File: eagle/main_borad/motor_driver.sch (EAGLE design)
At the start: 18 parts, among them IC1 MEGA8-AI

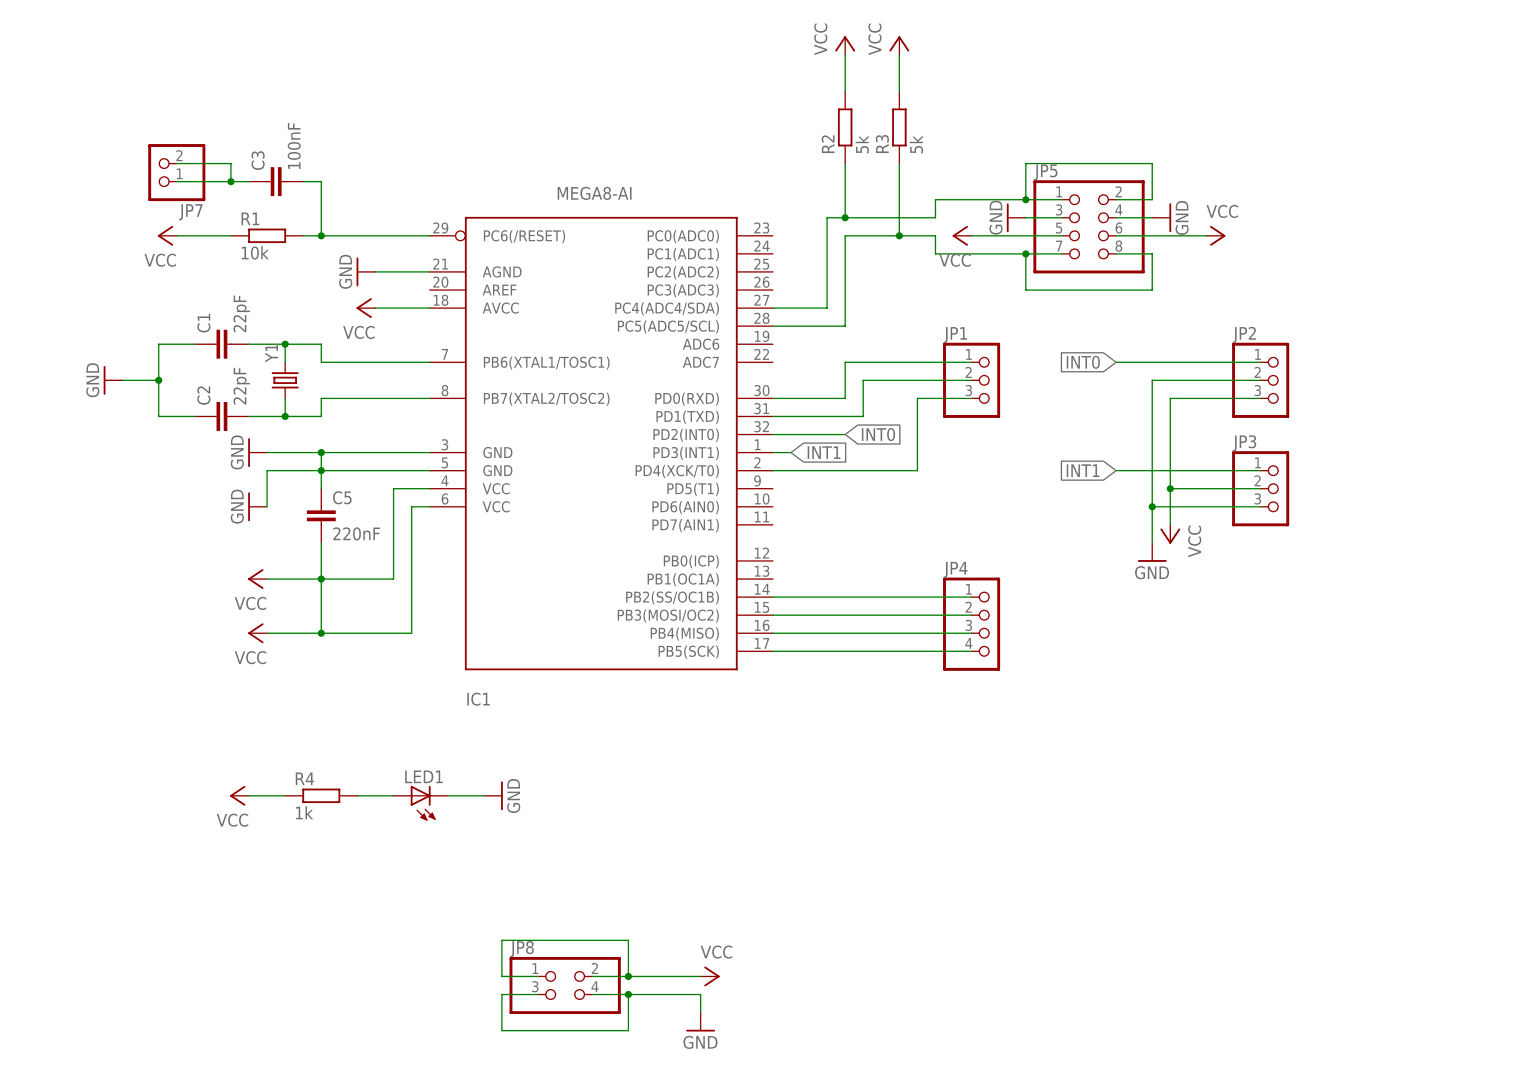
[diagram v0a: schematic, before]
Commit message: robot_driver updated
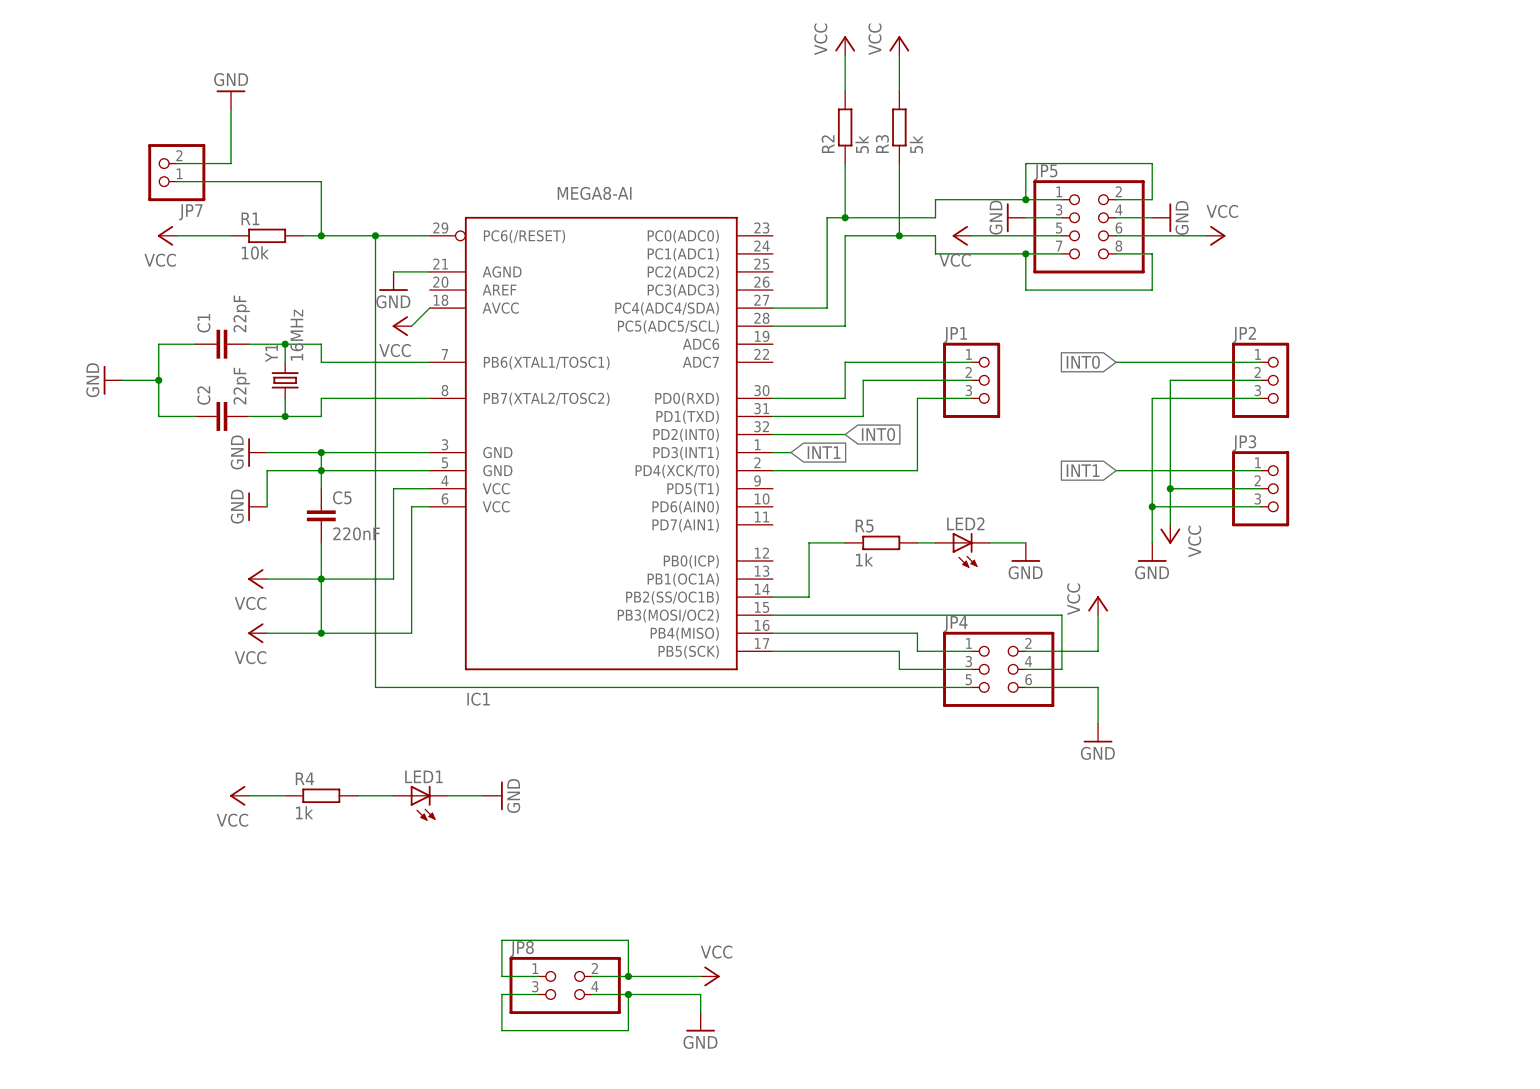
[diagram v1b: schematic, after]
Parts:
- removed C3: 100nF, SparkFun-Capacitors:CAP1206
- added LED2: (no value), adafruit:LEDCHIPLED_0805
- added R5: 1k, eagle-ltspice:R
- JP4: device pinhead:PINHD-1X4 -> pinhead:PINHD-2X3
- Y1: value (none) -> 16MHz
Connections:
- removed net N$15: IC1.PB2(SS/OC1B), JP4.1
- new net N$14: LED2.A, R5.2
- net GND: now also JP2.3, JP4.6, JP7.2, LED2.C; no longer JP2.2
- net N$12: now also JP4.3; no longer JP4.4
- net N$13: now also JP4.1; no longer JP4.3
- net N$4: now also IC1.PB2(SS/OC1B), R5.1; no longer C3.2, IC1.PC6(/RESET), R1.2
- net N$7: now also JP4.4; no longer JP4.2
- net RESET: now also IC1.PC6(/RESET), JP4.5, R1.2; no longer C3.1, JP7.2
- net VCC: now also JP2.2, JP4.2; no longer JP2.3

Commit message: otor_driver - led resistors updated
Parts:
- R4: value 1k -> 150k
- R5: value 1k -> 22k
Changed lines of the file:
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@@
 <part name="LED1" library="adafruit" deviceset="LED" device="CHIPLED_0805"/>
 <part name="GND9" library="supply1" deviceset="GND" device=""/>
-<part name="R4" library="eagle-ltspice" deviceset="R" device="" value="1k"/>
+<part name="R4" library="eagle-ltspice" deviceset="R" device="" value="150k"/>
 <part name="P+11" library="supply1" deviceset="VCC" device=""/>
 <part name="GND10" library="supply1" deviceset="GND" device=""/>
@@
 <part name="GND11" library="supply1" deviceset="GND" device=""/>
 <part name="P+12" library="supply1" deviceset="VCC" device=""/>
-<part name="R5" library="eagle-ltspice" deviceset="R" device="" value="1k"/>
+<part name="R5" library="eagle-ltspice" deviceset="R" device="" value="22k"/>
 <part name="LED2" library="adafruit" deviceset="LED" device="CHIPLED_0805"/>
 <part name="GND12" library="supply1" deviceset="GND" device=""/>

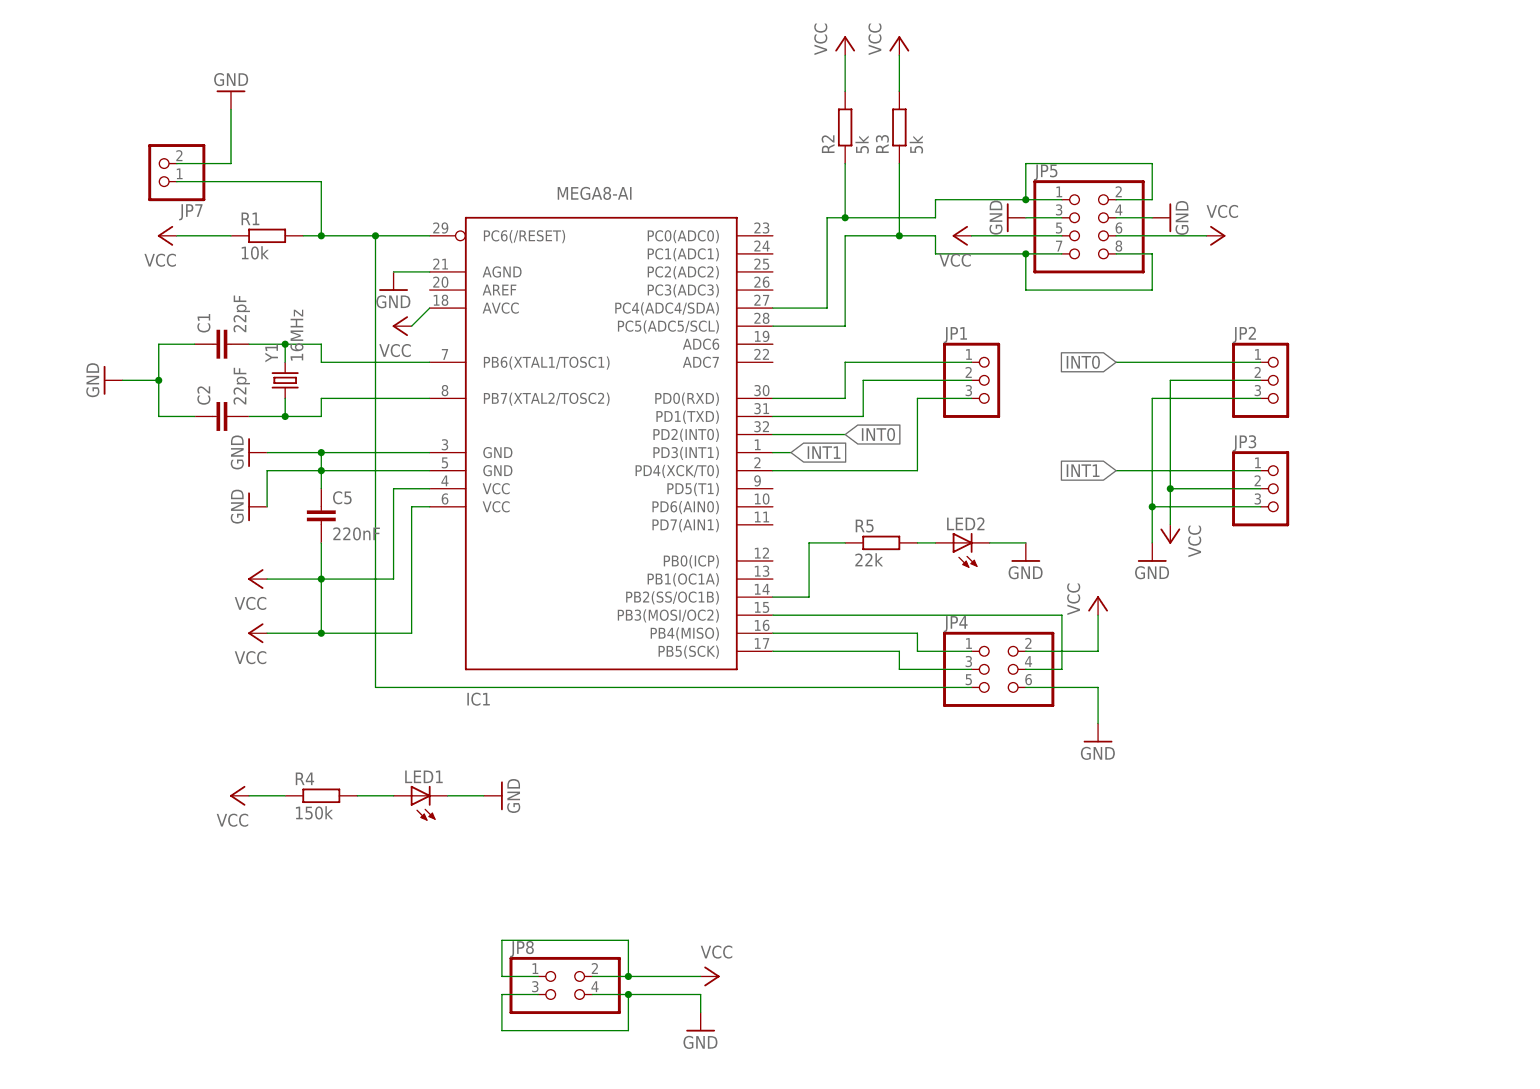
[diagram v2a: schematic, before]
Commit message: Repaired motor_driver PCB
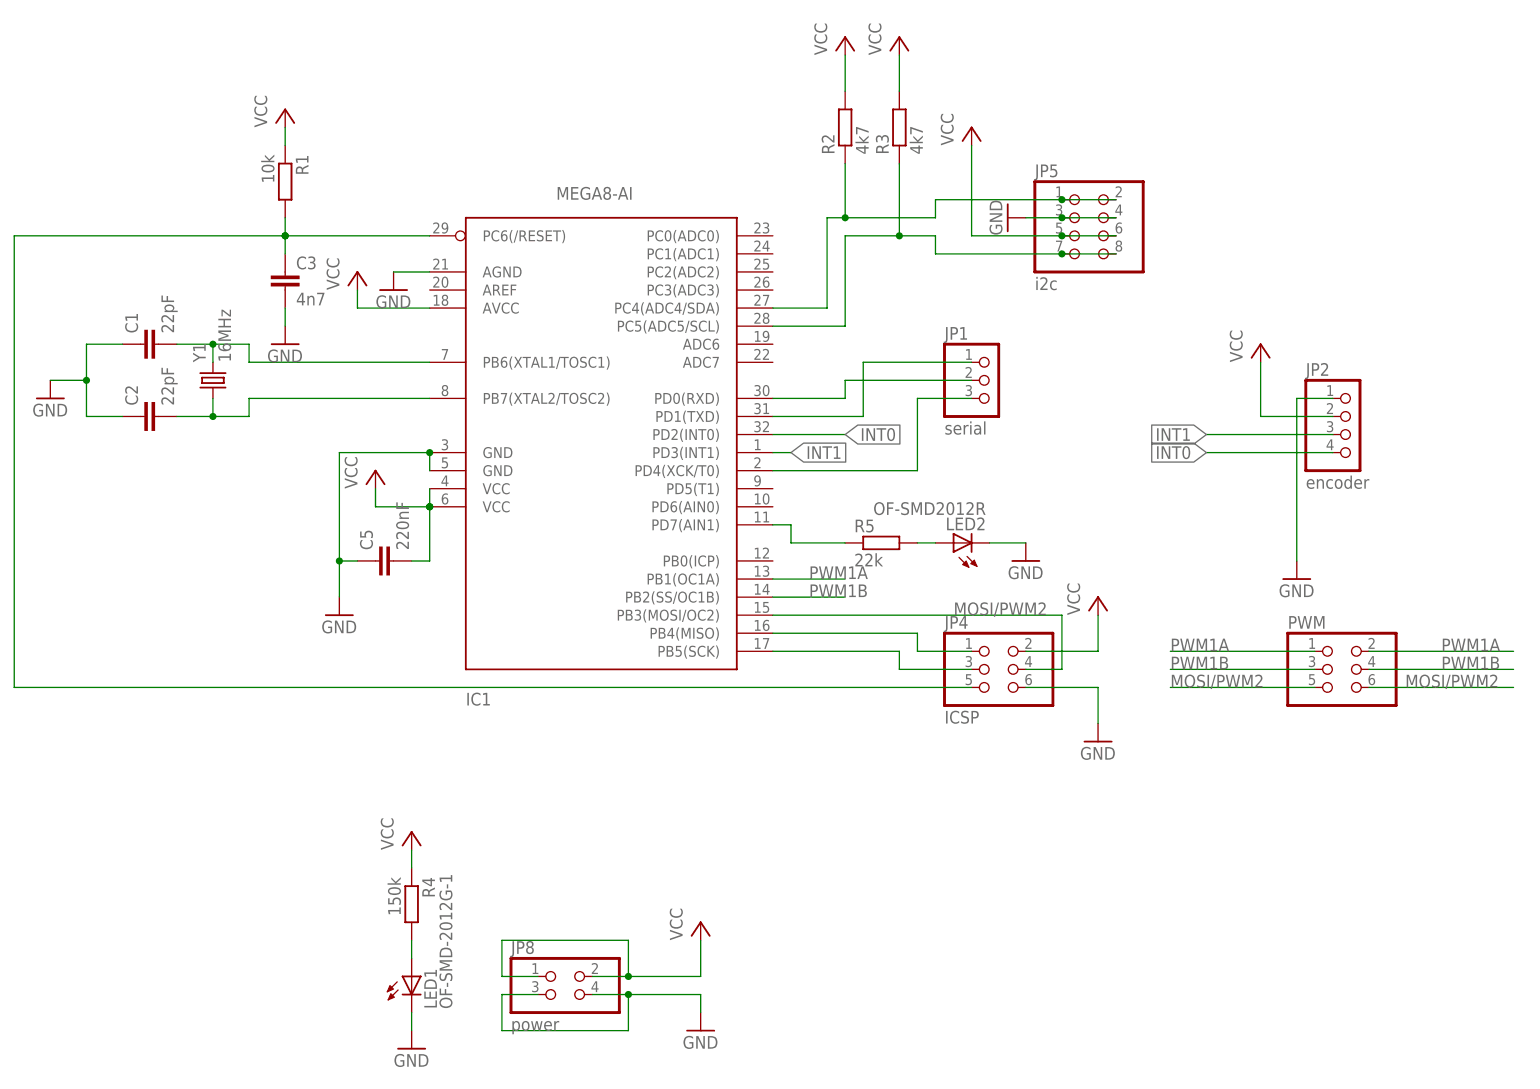
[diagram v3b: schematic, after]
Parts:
- removed JP3: (no value), pinhead:PINHD-1X3
- removed JP7: (no value), pinhead:PINHD-1X2
- added C3: 4n7, SparkFun-Capacitors:CAP1206
- added PWM: (no value), pinhead:PINHD-2X3
- JP1: value (none) -> serial; device pinhead:PINHD-1X3 -> pinhead-2:PINHD-1X03_2.54-S
- JP2: value (none) -> encoder; device pinhead:PINHD-1X3 -> pinhead-2:PINHD-1X04_2.54-S
- JP4: value (none) -> ICSP; device pinhead:PINHD-2X3 -> pinhead-2:PINHD-2X03_2.54
- JP5: value (none) -> i2c; device pinhead:PINHD-2X4 -> pinhead-2:PINHD-2X04_2.54
- JP8: value (none) -> power; device pinhead:PINHD-2X2 -> pinhead-2:PINHD-2X02_2.54
- LED1: value (none) -> OF-SMD-2012G-1; device adafruit:LEDCHIPLED_0805 -> adafruit:LED3MM
- LED2: value (none) -> OF-SMD2012R; device adafruit:LEDCHIPLED_0805 -> adafruit:LED3MM
- R2, R3: value 5k -> 4k7
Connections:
- removed net N$7: IC1.PB3(MOSI/OC2), JP4.4
- new net MOSI/PWM2: IC1.PB3(MOSI/OC2), JP4.4, PWM.5, PWM.6
- new net PWM1A: IC1.PB1(OC1A), PWM.1, PWM.2
- new net PWM1B: IC1.PB2(SS/OC1B), PWM.3, PWM.4
- net GND: now also C3.2, JP2.1; no longer JP2.3, JP3.3, JP7.2
- net INT0: now also JP2.4; no longer JP2.1
- net INT1: now also JP2.3; no longer JP3.1
- net N$1: now also JP1.1; no longer JP1.2
- net N$4: now also IC1.PD7(AIN1); no longer IC1.PB2(SS/OC1B)
- net N$5: now also JP1.2; no longer JP1.1
- net RESET: now also C3.1; no longer JP7.1
- net VCC: no longer JP3.2
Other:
- moved on the sheet: C1, C2, C5, LED1, R1, R4, Y1
